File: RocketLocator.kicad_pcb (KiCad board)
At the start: 4 copper layers, 54 x 25 mm, 118 parts, among them J1 USB_C, J12 Battery / Switch, J2 Deploy Ch1 / Ch2, J3 Battery-, J4 Deploy Ch3 / Ch4, J7 U.FL-R-SMT(01), J8 Conn_ST_STDC14, Q1 2N7002KN, Q3 BSS84, Q4 PMXB43UNE, Q5 PMXB43UNE, Q6 PMXB43UNE, Q7 PMXB43UNE, U1 TPS22950YBHR, U11 PAM8904EGPR, U12 74HCS00, U13 DMP2021UFDF, U14 ISM6HG256XTR, U15 TPS22950YBHR, U16 MS5611-01BA, U17 MX25L6436F, U18 BQ25185DLHR, U2 SAM-M10Q-00B, U3 DRV5032DUDMRR, U4 CH340N, U5 STM32WL5MOCH6TR, U6 TPS22950YBHR, U7 RT9080-33GJ5, U8 TPS22950YBHR, U9 TPS22950YBHR

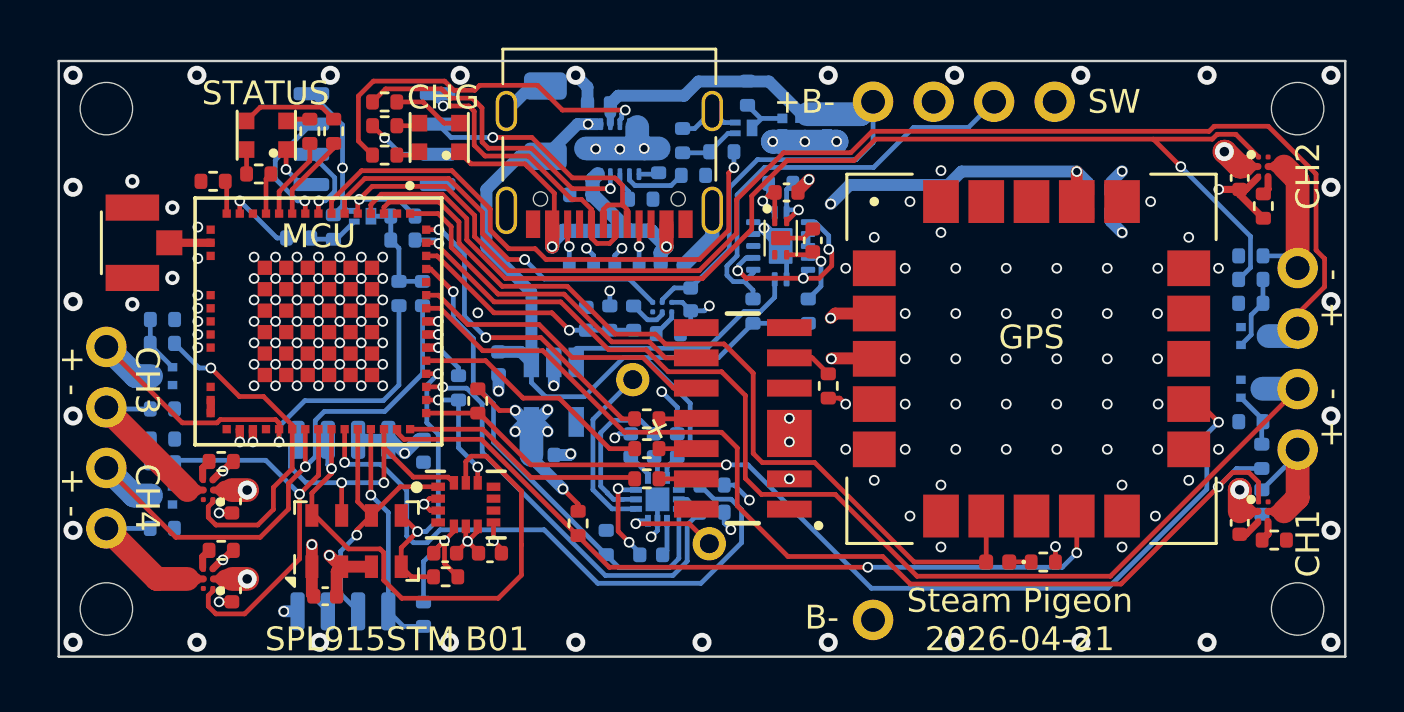
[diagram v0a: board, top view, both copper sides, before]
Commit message: Place magnetometer U19 and reroute (Frank, after KiCad crash)
Co-Authored-By: Claude Opus 5.5 (1M context) <noreply@anthropic.com>
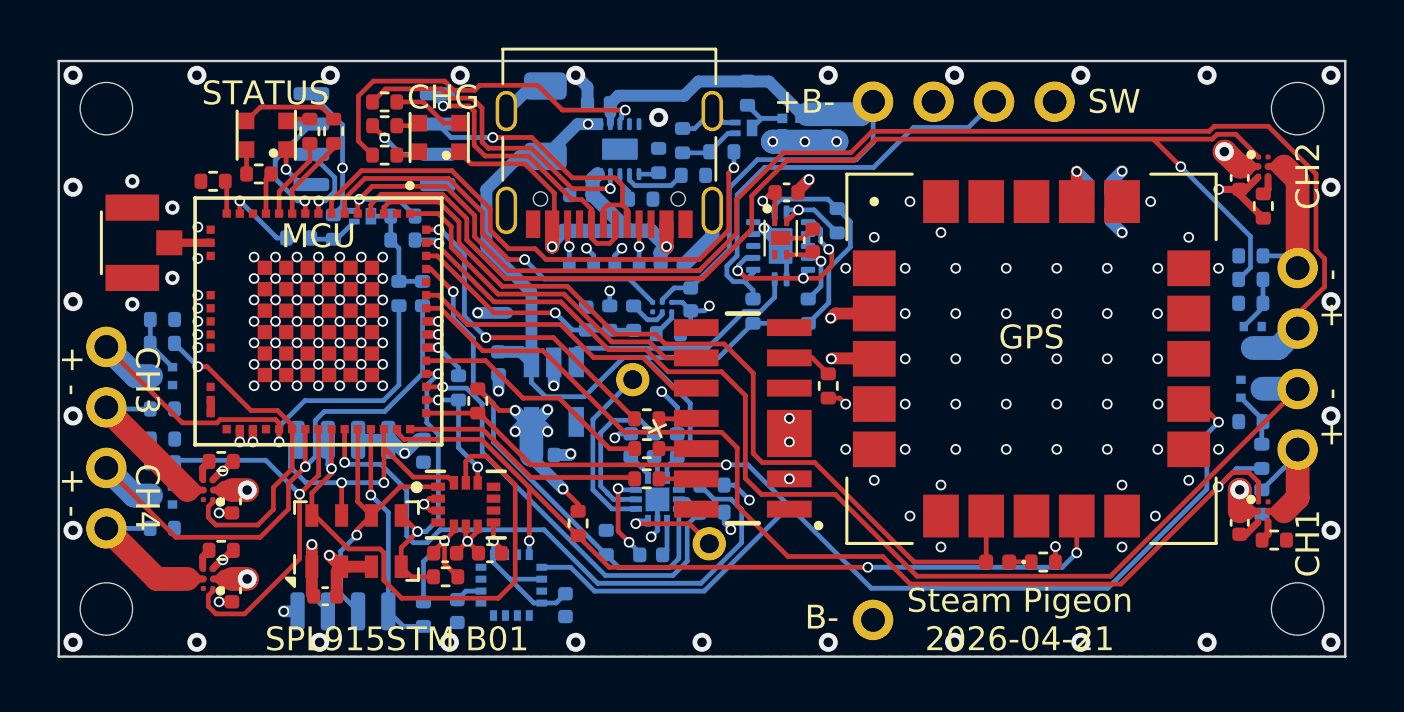
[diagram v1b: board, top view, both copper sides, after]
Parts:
- added C37: 10uF, Capacitor_SMD:C_0402_1005Metric, B.Cu at (36.7, 43.1)
- added C38: 1uF, Capacitor_SMD:C_0402_1005Metric, B.Cu at (41.3, 42.8)
- added U19: MMC5983MA, Package_LGA:LGA-16_3x3mm_P0.5mm, B.Cu at (39.0, 42.0)
- moved R30 2.84 mm to (52.7, 26.7), turned to -90 degrees
- moved Q5 0.07 mm to (70.1, 31.6), turned to 180 degrees
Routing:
- net $SCL: track 42.1 -> 54.4 mm
- net +3V3: track 56.1 -> 61.5 mm, vias 21 -> 20
- net $SDA: track 32.8 -> 35.6 mm, vias 2 -> 3
- net GND: track 54.4 -> 51.6 mm, vias 171 -> 168
- net Net-(U19-CAP): track 0.00 -> 1.14 mm
- net SYS: track 48.3 -> 47.2 mm
- net DS2: track 58.3 -> 59.1 mm
- net Net-(Q5-G): track 3.13 -> 2.31 mm
- net Net-(U3-OUT1): track 2.57 -> 3.25 mm

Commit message: Restore post-crash PCB fixes from PR #13
KiCad crashed during U19 placement and the saved board lost several
fixes that were merged in PR #13. Re-apply them without touching the
new placement or routing:

- Re-sync footprints (0402 R/C/LED library updates, hidden Q4-Q7 and
  R45-R56 reference labels, LGA-92 courtyard) from main, keeping the
  current position, side and rotation of every part.
- Remove the dangling DEPLOY1+..4+ stub tracks and the orphan SYS via.
- Refill zones.

DRC: 14 intentional warnings (as on main, minus two silk items) and
1 unconnected item: Q5 pad 2 (GND) sits in an isolated B.Cu island
after Q5 was rotated to 180 degrees. Left for manual rerouting.

Co-Authored-By: Claude Opus 5.5 (1M context) <noreply@anthropic.com>
Claude-Session: https://claude.ai/code/session_01FYY8Uv6gBjRSv3QTZNtnYK
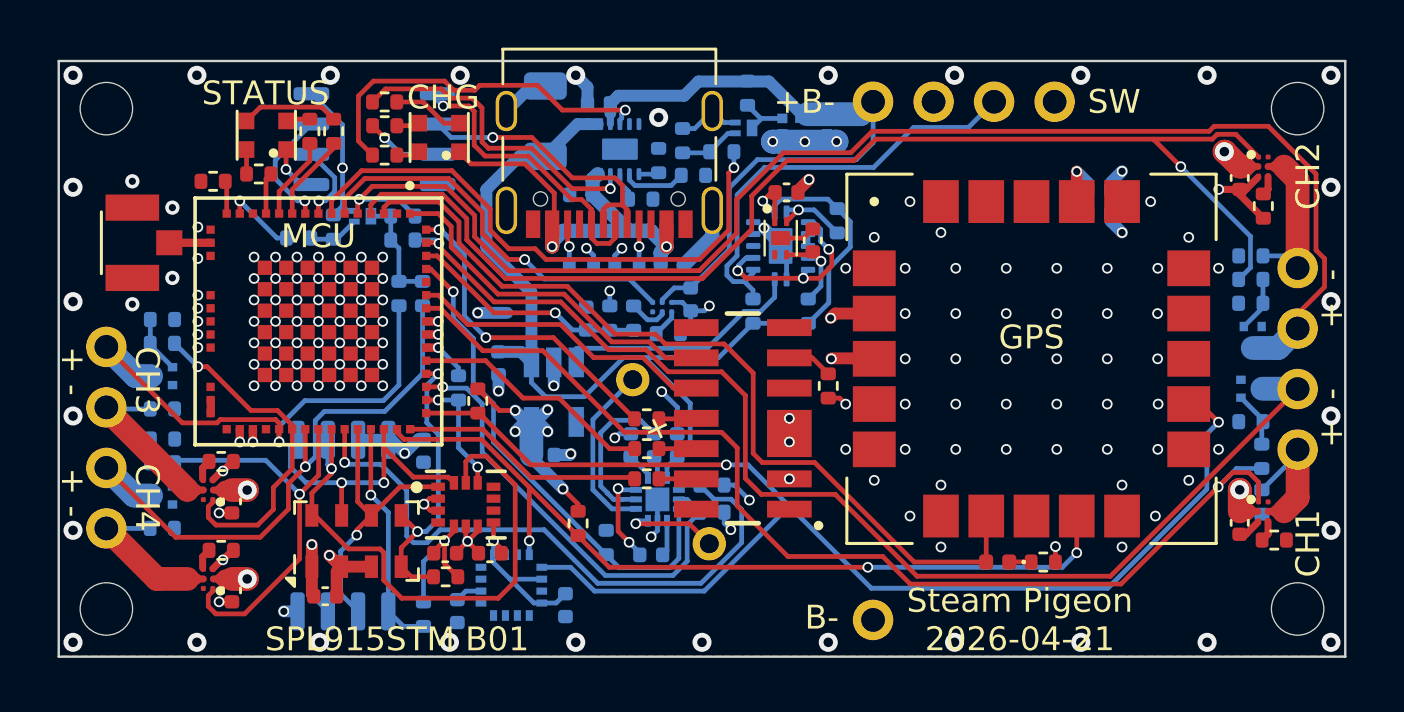
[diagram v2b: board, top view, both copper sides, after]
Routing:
- net SYS: vias 2 -> 1

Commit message: Board: U18 thermal vias, straight Ch4 DPWR feed (Frank)
Co-Authored-By: Claude Opus 5.5 (1M context) <noreply@anthropic.com>
Claude-Session: https://claude.ai/code/session_01FYY8Uv6gBjRSv3QTZNtnYK
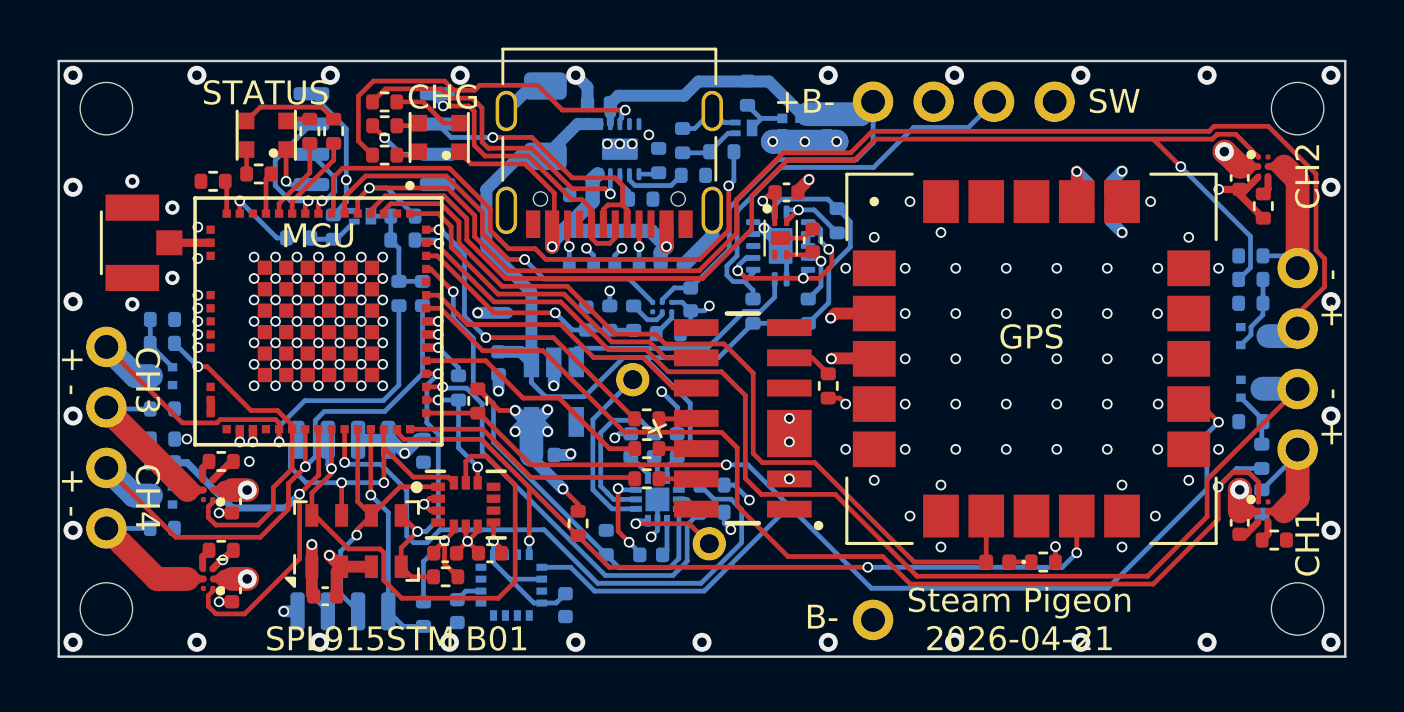
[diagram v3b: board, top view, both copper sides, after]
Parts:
- moved Q5 0.07 mm to (70.1, 31.5), turned to -90 degrees
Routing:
- net DPWR: track 93.6 -> 86.5 mm
- net DS2: track 59.1 -> 58.0 mm
- net +5V: track 18.3 -> 17.3 mm
- net DS1: track 50.3 -> 51.2 mm
- net Net-(Q5-G): track 2.31 -> 3.14 mm
- net D1: track 46.2 -> 47.0 mm
- net DARM: track 23.7 -> 24.3 mm
- net GND: vias 168 -> 172

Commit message: Board: place spaced J12, remove J3 (Frank)
J12 at (66.88, 21.71) rot -90 with the new 1x06 outline: +BATT stays
at x=54.18, GND/MSW/GND at 61.80/64.34/66.88. MSW rerouted, J3 deleted.
DRC: 0 errors, 0 unconnected, 0 parity issues, 14 intentional warnings.

Co-Authored-By: Claude Opus 5.5 (1M context) <noreply@anthropic.com>
Claude-Session: https://claude.ai/code/session_01FYY8Uv6gBjRSv3QTZNtnYK
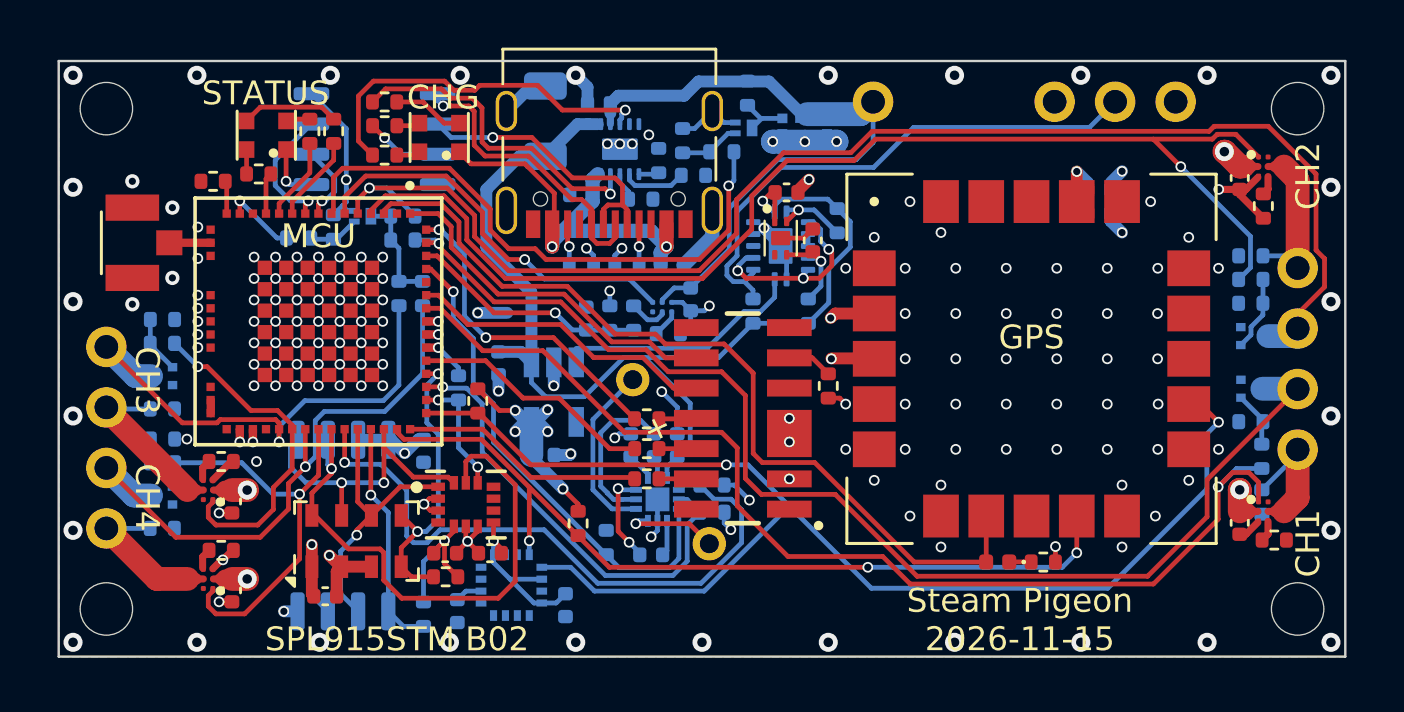
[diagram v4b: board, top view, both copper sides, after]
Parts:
- removed J3: Battery-, Custom:PinHeader_1x01_P2.54mm_Vertical
- J12: footprint Custom:PinHeader_1x04_P2.54mm_Vertical -> Custom:PinHeader_1x06_P2.54mm_Vertical_Pos4-5_Empty
- moved J12 5.08 mm to (66.9, 21.7)
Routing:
- net MSW: track 17.9 -> 23.0 mm
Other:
- board text added: "SPL915STM B02"
- board text added: "Steam Pigeon 2026-11-15"
- board text removed: "SPL915STM B01"
- board text removed: "Steam Pigeon 2026-04-21"

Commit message: Add Steam Pigeon app logo to bottom silkscreen
New footprint Custom:SteamPigeon_Logo_13mm (12.8 x 13.1 mm, B.SilkS when
placed on the back) traced from the steam-pigeon-ios AppIcon: filled
artwork with the drawing's outlines as knockouts, min line/gap ~0.18 mm.
Board-only, excluded from BOM/CPL, courtyard not required.
Placed as G1 on the bottom at (58.8, 32.6) in the open area left of U12.
DRC unchanged from main.

Co-Authored-By: Claude Opus 5.5 (1M context) <noreply@anthropic.com>
Claude-Session: https://claude.ai/code/session_012mcqyg5z3e1rRwnuuyV256
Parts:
- added G1: SteamPigeon_Logo_13mm, Custom:SteamPigeon_Logo_13mm, B.Cu at (58.8, 32.6)

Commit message: Add small Steam Pigeon logo to top silkscreen
New footprint Custom:SteamPigeon_Logo_3mm (2.8 x 3.0 mm): a simplified
silhouette of the app logo (rocket, wings, exhaust cloud, window
knockout) with stars and fine interior lines dropped so every line and
gap is at least 0.15 mm. Board-only, excluded from BOM/CPL.
Placed as G2 on the top at (67.4, 43.1), right of the "Steam Pigeon"
text block. DRC unchanged (14 pre-existing violations).

Co-Authored-By: Claude Opus 5.5 (1M context) <noreply@anthropic.com>
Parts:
- added G2: SteamPigeon_Logo_3mm, Custom:SteamPigeon_Logo_3mm, F.Cu at (67.4, 43.1)

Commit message: Board: logo placement tweaks (Frank)
Co-Authored-By: Claude Opus 5.5 (1M context) <noreply@anthropic.com>
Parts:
- moved G1 1.41 mm to (60.0, 33.3)
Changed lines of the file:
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@@
 	(footprint "Custom:SteamPigeon_Logo_13mm"
 		(layer "B.Cu")
-		(at 58.8 32.6 180)
+		(at 60.03 33.28 180)
 		(descr "Steam Pigeon app logo (winged rocket), silkscreen art")
 		(tags "logo steam pigeon rocket")
